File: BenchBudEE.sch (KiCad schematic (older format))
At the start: 0 parts

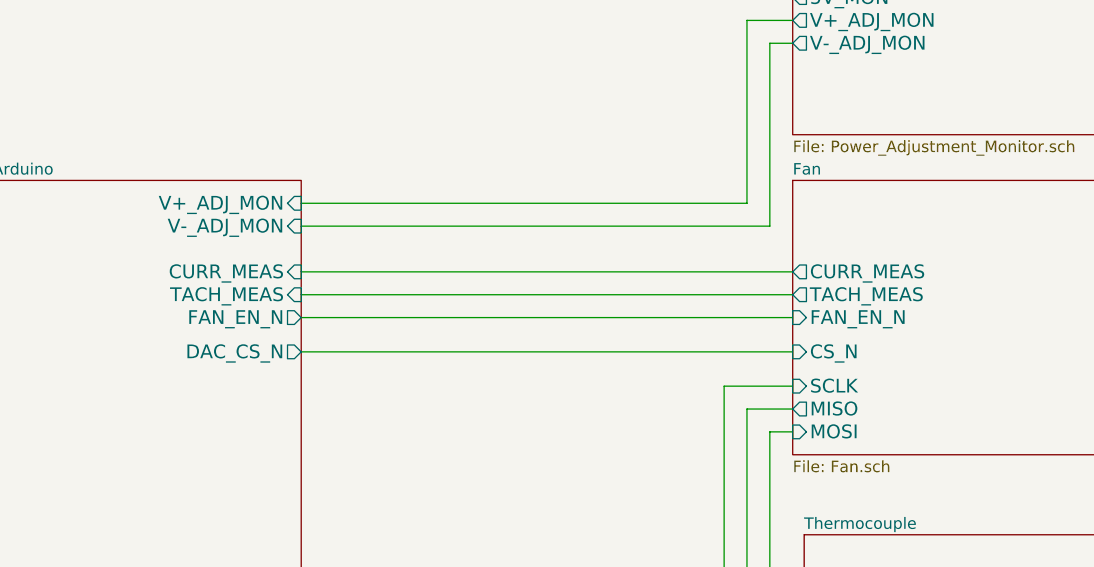
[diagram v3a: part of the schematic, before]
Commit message: Modified the FAN module and corresponding pins in Arduino module
1) Added FAN_MODE
2) Changed FAN_EN_N to FAN_PWM
3) Used one of the digital PWM pins for FAN_PWM
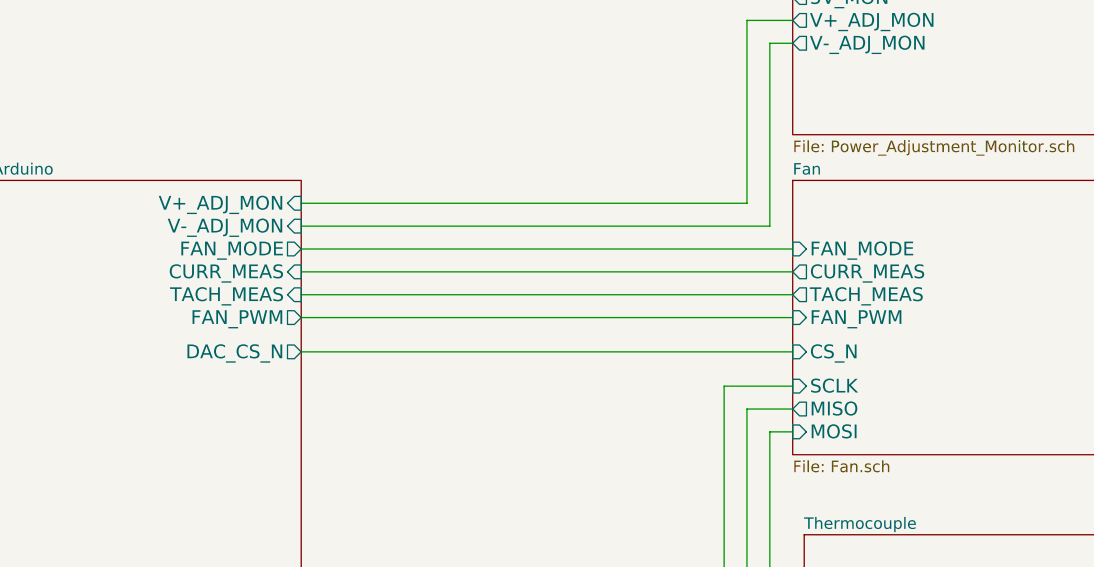
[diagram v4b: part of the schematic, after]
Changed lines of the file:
@@
 Sheet 1 9
 Title ""
-Date "10 feb 2014"
+Date "11 feb 2014"
 Rev ""
 Comp ""
@@
 F4 "SCLK" O R 5350 4100 60
 F5 "TACH_MEAS" I R 5350 2450 60
-F6 "FAN_EN_N" O R 5350 2550 60
-F7 "CURR_MEAS" I R 5350 2350 60
-F8 "RELAY+" O R 5350 5000 60
-F9 "RELAY-" O R 5350 5150 60
-F10 "LED_EN_PWM" O R 5350 6050 60
-F11 "V+_ADJ_MON" I R 5350 2050 60
-F12 "V-_ADJ_MON" I R 5350 2150 60
-F13 "DAC_CS_N" O R 5350 2700 60
-F14 "ADC_CS_N" O R 5350 4300 60
+F6 "CURR_MEAS" I R 5350 2350 60
+F7 "RELAY+" O R 5350 5000 60
+F8 "RELAY-" O R 5350 5150 60
+F9 "LED_EN_PWM" O R 5350 6050 60
+F10 "V+_ADJ_MON" I R 5350 2050 60
+F11 "V-_ADJ_MON" I R 5350 2150 60
+F12 "DAC_CS_N" O R 5350 2700 60
+F13 "ADC_CS_N" O R 5350 4300 60
+F14 "FAN_PWM" O R 5350 2550 60
+F15 "FAN_MODE" O R 5350 2250 60
 $EndSheet
 $Sheet
@@
 F8 "TACH_MEAS" O L 7500 2450 60
 F9 "CURR_MEAS" O L 7500 2350 60
-F10 "FAN_EN_N" I L 7500 2550 60
-F11 "PWR-" O R 9450 2300 60
+F10 "PWR-" O R 9450 2300 60
+F11 "FAN_PWM" I L 7500 2550 60
+F12 "FAN_MODE" I L 7500 2250 60
 $EndSheet
 $Sheet
@@
 Wire Wire Line
 	5350 4300 7550 4300
+Wire Wire Line
+	5350 2250 7500 2250
 $EndSCHEMATC

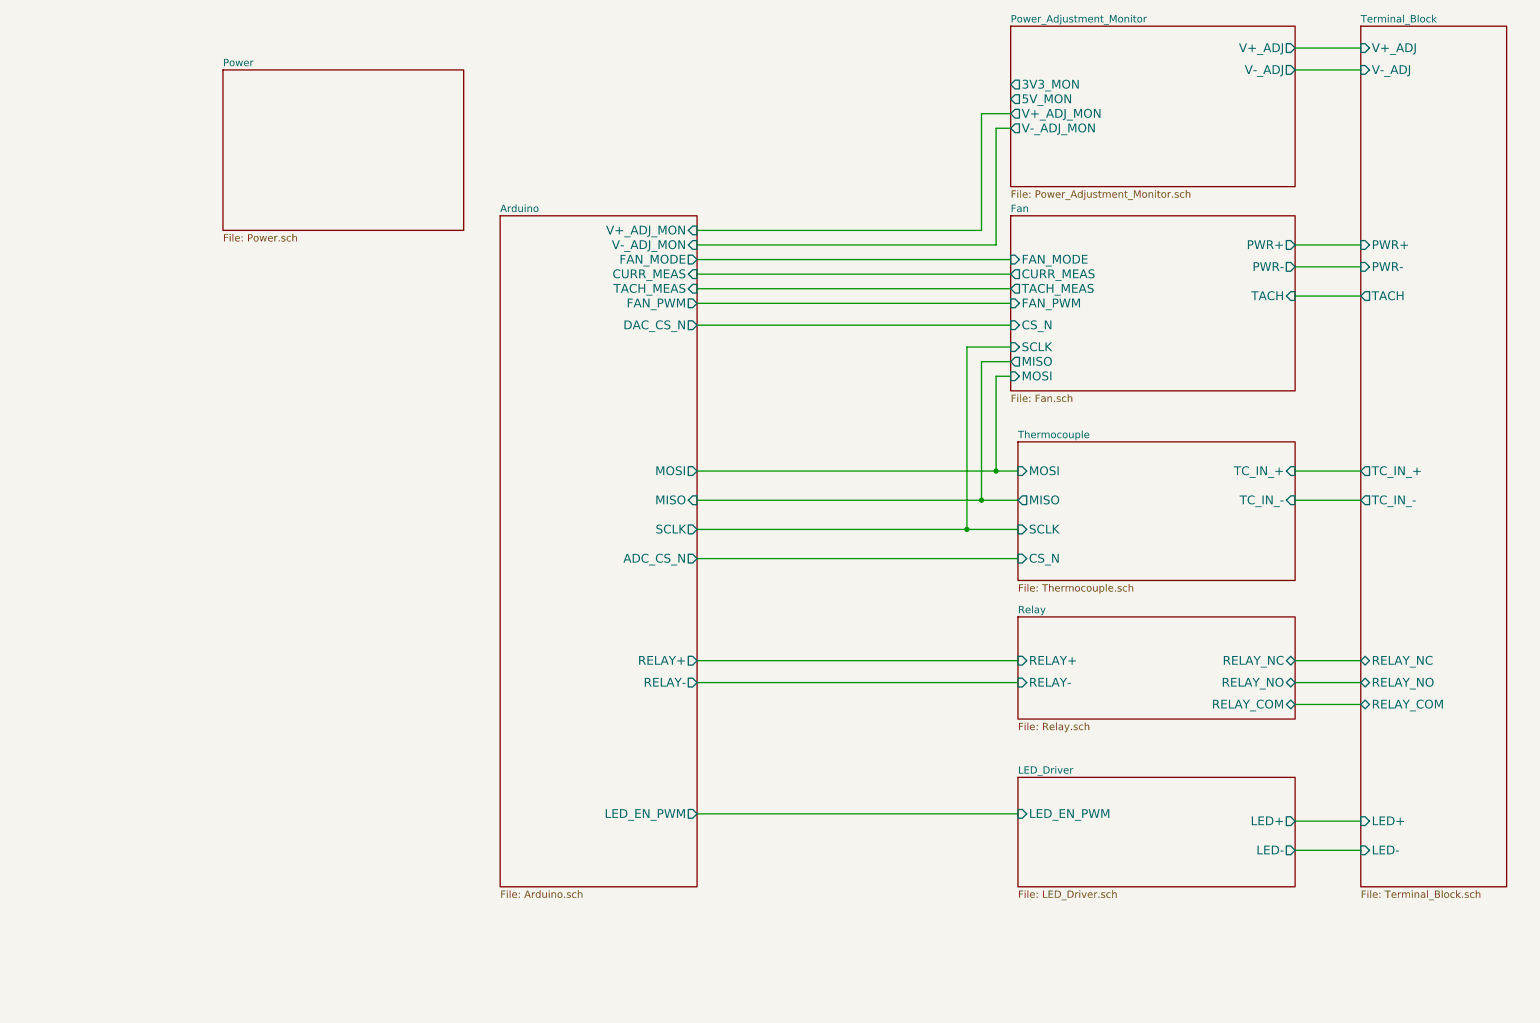
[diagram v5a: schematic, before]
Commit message: THERMOCOUPLE 02-22-2014
Associated and placed PCB footprints of thermocouple modules in layout
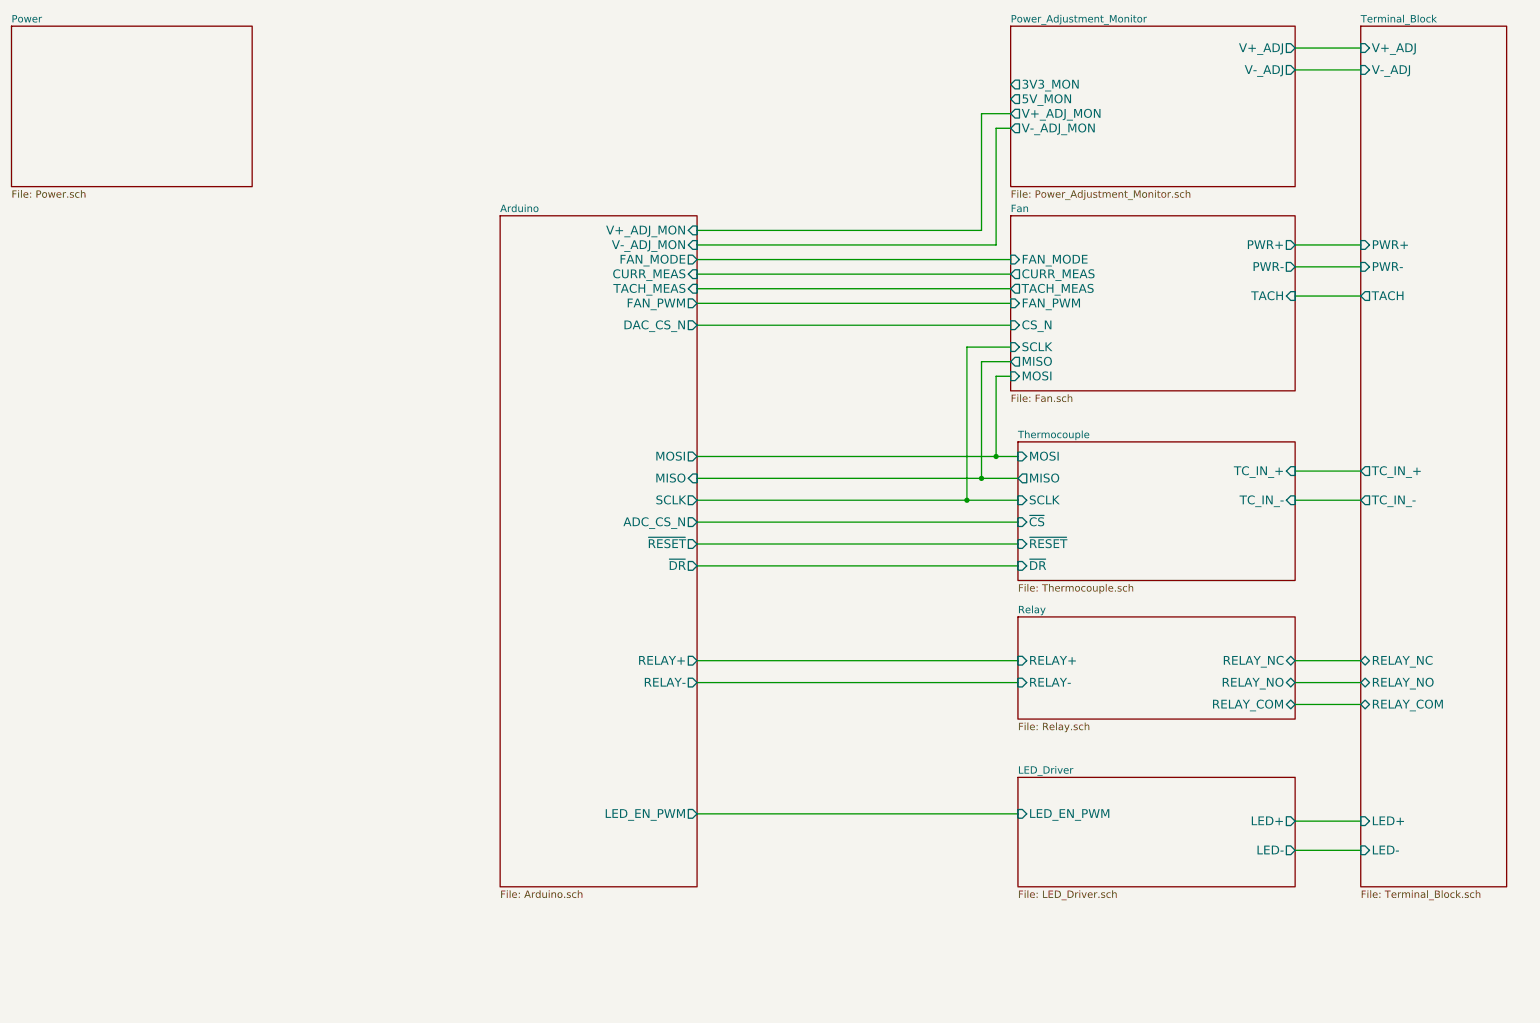
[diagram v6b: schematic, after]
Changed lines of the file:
@@
 Sheet 1 9
 Title ""
-Date "20 feb 2014"
+Date "23 feb 2014"
 Rev ""
 Comp ""
@@
 F0 "Arduino" 50
 F1 "Arduino.sch" 50
-F2 "MOSI" O R 5350 3700 60
-F3 "MISO" I R 5350 3900 60
-F4 "SCLK" O R 5350 4100 60
+F2 "MOSI" O R 5350 3600 60
+F3 "MISO" I R 5350 3750 60
+F4 "SCLK" O R 5350 3900 60
 F5 "TACH_MEAS" I R 5350 2450 60
 F6 "CURR_MEAS" I R 5350 2350 60
@@
 F11 "V-_ADJ_MON" I R 5350 2150 60
 F12 "DAC_CS_N" O R 5350 2700 60
-F13 "ADC_CS_N" O R 5350 4300 60
+F13 "ADC_CS_N" O R 5350 4050 60
 F14 "FAN_PWM" O R 5350 2550 60
 F15 "FAN_MODE" O R 5350 2250 60
+F16 "~RESET" O R 5350 4200 60
+F17 "~DR" O R 5350 4350 60
 $EndSheet
 $Sheet
@@
 F2 "TC_IN_+" I R 9450 3700 60
 F3 "TC_IN_-" I R 9450 3900 60
-F4 "MOSI" I L 7550 3700 60
-F5 "MISO" O L 7550 3900 60
-F6 "SCLK" I L 7550 4100 60
-F7 "CS_N" I L 7550 4300 60
+F4 "MOSI" I L 7550 3600 60
+F5 "MISO" O L 7550 3750 60
+F6 "SCLK" I L 7550 3900 60
+F7 "~CS" I L 7550 4050 60
+F8 "~RESET" I L 7550 4200 60
+F9 "~DR" I L 7550 4350 60
 $EndSheet
 $Sheet
-S 2100 950  1650 1100
+S 650  650  1650 1100
 U 52EE0B23
 F0 "Power" 50
@@
 	5350 5150 7550 5150
 Wire Wire Line
-	5350 3700 7550 3700
-Wire Wire Line
-	5350 3900 7550 3900
-Wire Wire Line
-	5350 4100 7550 4100
-Wire Wire Line
 	7500 3050 7400 3050
-Wire Wire Line
-	7400 3050 7400 3700
-Connection ~ 7400 3700
 Wire Wire Line
 	7500 2950 7300 2950
 Wire Wire Line
-	7300 2950 7300 3900
-Connection ~ 7300 3900
-Wire Wire Line
 	7500 2850 7200 2850
-Wire Wire Line
-	7200 2850 7200 4100
-Connection ~ 7200 4100
 Wire Wire Line
 	7550 6050 5350 6050
@@
 	5350 2700 7500 2700
 Wire Wire Line
-	5350 4300 7550 4300
+	5350 2250 7500 2250
 Wire Wire Line
-	5350 2250 7500 2250
+	5350 3600 7550 3600
+Wire Wire Line
+	5350 3750 7550 3750
+Wire Wire Line
+	5350 3900 7550 3900
+Wire Wire Line
+	5350 4050 7550 4050
+Wire Wire Line
+	7400 3050 7400 3600
+Connection ~ 7400 3600
+Wire Wire Line
+	7300 2950 7300 3750
+Connection ~ 7300 3750
+Wire Wire Line
+	7200 2850 7200 3900
+Connection ~ 7200 3900
+Wire Wire Line
+	5350 4200 7550 4200
+Wire Wire Line
+	5350 4350 7550 4350
 $EndSCHEMATC

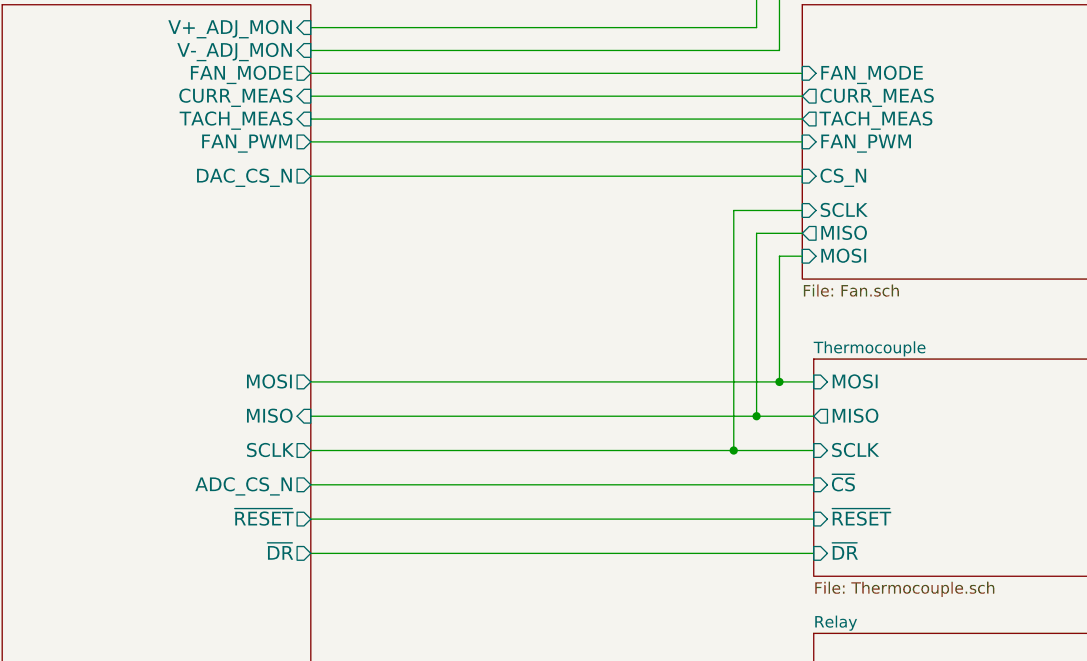
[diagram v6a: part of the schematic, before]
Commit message: Fan Controller Module
1) Created and associated the footprints of fan controller module
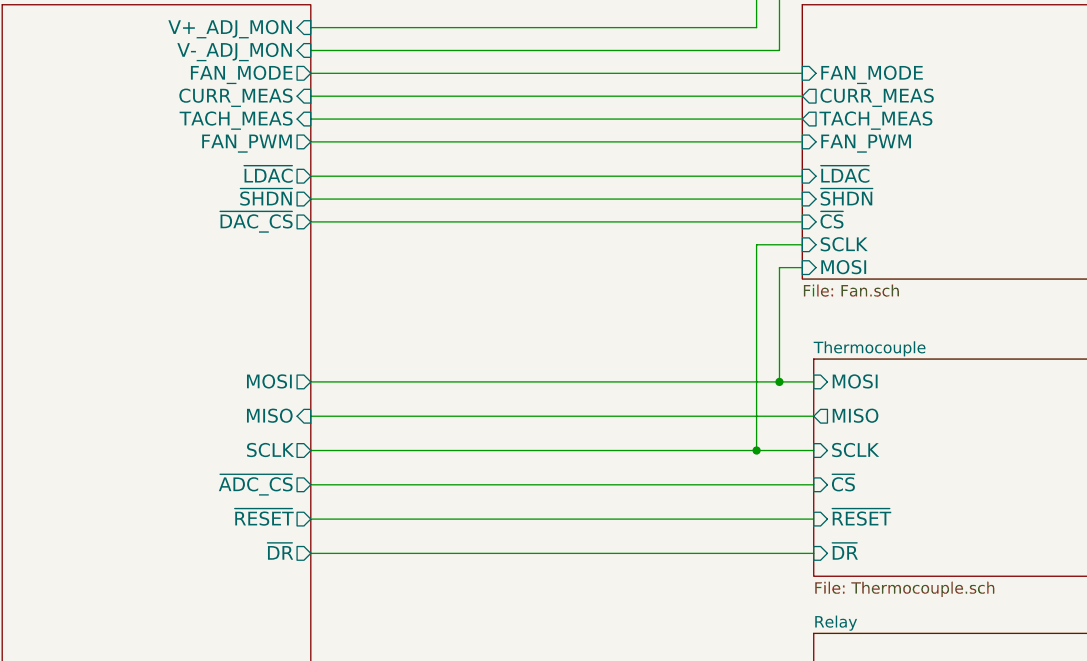
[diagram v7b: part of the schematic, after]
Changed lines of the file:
@@
 Sheet 1 9
 Title ""
-Date "23 feb 2014"
+Date "24 feb 2014"
 Rev ""
 Comp ""
@@
 F10 "V+_ADJ_MON" I R 5350 2050 60
 F11 "V-_ADJ_MON" I R 5350 2150 60
-F12 "DAC_CS_N" O R 5350 2700 60
-F13 "ADC_CS_N" O R 5350 4050 60
-F14 "FAN_PWM" O R 5350 2550 60
-F15 "FAN_MODE" O R 5350 2250 60
-F16 "~RESET" O R 5350 4200 60
-F17 "~DR" O R 5350 4350 60
+F12 "FAN_PWM" O R 5350 2550 60
+F13 "FAN_MODE" O R 5350 2250 60
+F14 "~RESET" O R 5350 4200 60
+F15 "~DR" O R 5350 4350 60
+F16 "~LDAC" O R 5350 2700 60
+F17 "~SHDN" O R 5350 2800 60
+F18 "~DAC_CS" O R 5350 2900 60
+F19 "~ADC_CS" O R 5350 4050 60
 $EndSheet
 $Sheet
@@
 F2 "PWR+" O R 9450 2150 60
 F3 "TACH" I R 9450 2500 60
-F4 "MOSI" I L 7500 3050 60
-F5 "MISO" O L 7500 2950 60
-F6 "CS_N" I L 7500 2700 60
-F7 "SCLK" I L 7500 2850 60
-F8 "TACH_MEAS" O L 7500 2450 60
-F9 "CURR_MEAS" O L 7500 2350 60
-F10 "PWR-" O R 9450 2300 60
-F11 "FAN_PWM" I L 7500 2550 60
-F12 "FAN_MODE" I L 7500 2250 60
+F4 "MOSI" I L 7500 3100 60
+F5 "SCLK" I L 7500 3000 60
+F6 "TACH_MEAS" O L 7500 2450 60
+F7 "CURR_MEAS" O L 7500 2350 60
+F8 "PWR-" O R 9450 2300 60
+F9 "FAN_PWM" I L 7500 2550 60
+F10 "FAN_MODE" I L 7500 2250 60
+F11 "~LDAC" I L 7500 2700 60
+F12 "~SHDN" I L 7500 2800 60
+F13 "~CS" I L 7500 2900 60
 $EndSheet
 $Sheet
@@
 	5350 5150 7550 5150
 Wire Wire Line
-	7500 3050 7400 3050
-Wire Wire Line
-	7500 2950 7300 2950
-Wire Wire Line
-	7500 2850 7200 2850
+	7500 3100 7400 3100
+Wire Wire Line
+	7500 3000 7300 3000
 Wire Wire Line
 	7550 6050 5350 6050
@@
 	7400 1350 7500 1350
 Wire Wire Line
+	5350 2900 7500 2900
+Wire Wire Line
+	5350 2250 7500 2250
+Wire Wire Line
+	5350 3600 7550 3600
+Wire Wire Line
+	5350 3750 7550 3750
+Wire Wire Line
+	5350 3900 7550 3900
+Wire Wire Line
+	5350 4050 7550 4050
+Wire Wire Line
+	7400 3100 7400 3600
+Connection ~ 7400 3600
+Wire Wire Line
+	7300 3000 7300 3900
+Connection ~ 7300 3900
+Wire Wire Line
+	5350 4200 7550 4200
+Wire Wire Line
+	5350 4350 7550 4350
+Wire Wire Line
 	5350 2700 7500 2700
 Wire Wire Line
-	5350 2250 7500 2250
-Wire Wire Line
-	5350 3600 7550 3600
-Wire Wire Line
-	5350 3750 7550 3750
-Wire Wire Line
-	5350 3900 7550 3900
-Wire Wire Line
-	5350 4050 7550 4050
-Wire Wire Line
-	7400 3050 7400 3600
-Connection ~ 7400 3600
-Wire Wire Line
-	7300 2950 7300 3750
-Connection ~ 7300 3750
-Wire Wire Line
-	7200 2850 7200 3900
-Connection ~ 7200 3900
-Wire Wire Line
-	5350 4200 7550 4200
-Wire Wire Line
-	5350 4350 7550 4350
+	5350 2800 7500 2800
 $EndSCHEMATC
